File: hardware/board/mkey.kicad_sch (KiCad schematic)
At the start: 163 parts, among them J1 USB_C_REP_2.0, J2 24 pin LCD FPC connector, SW1 SW_Push, SW2 SW_Push, U1 ESP32-S3-WROOM-1, U5 SY8088

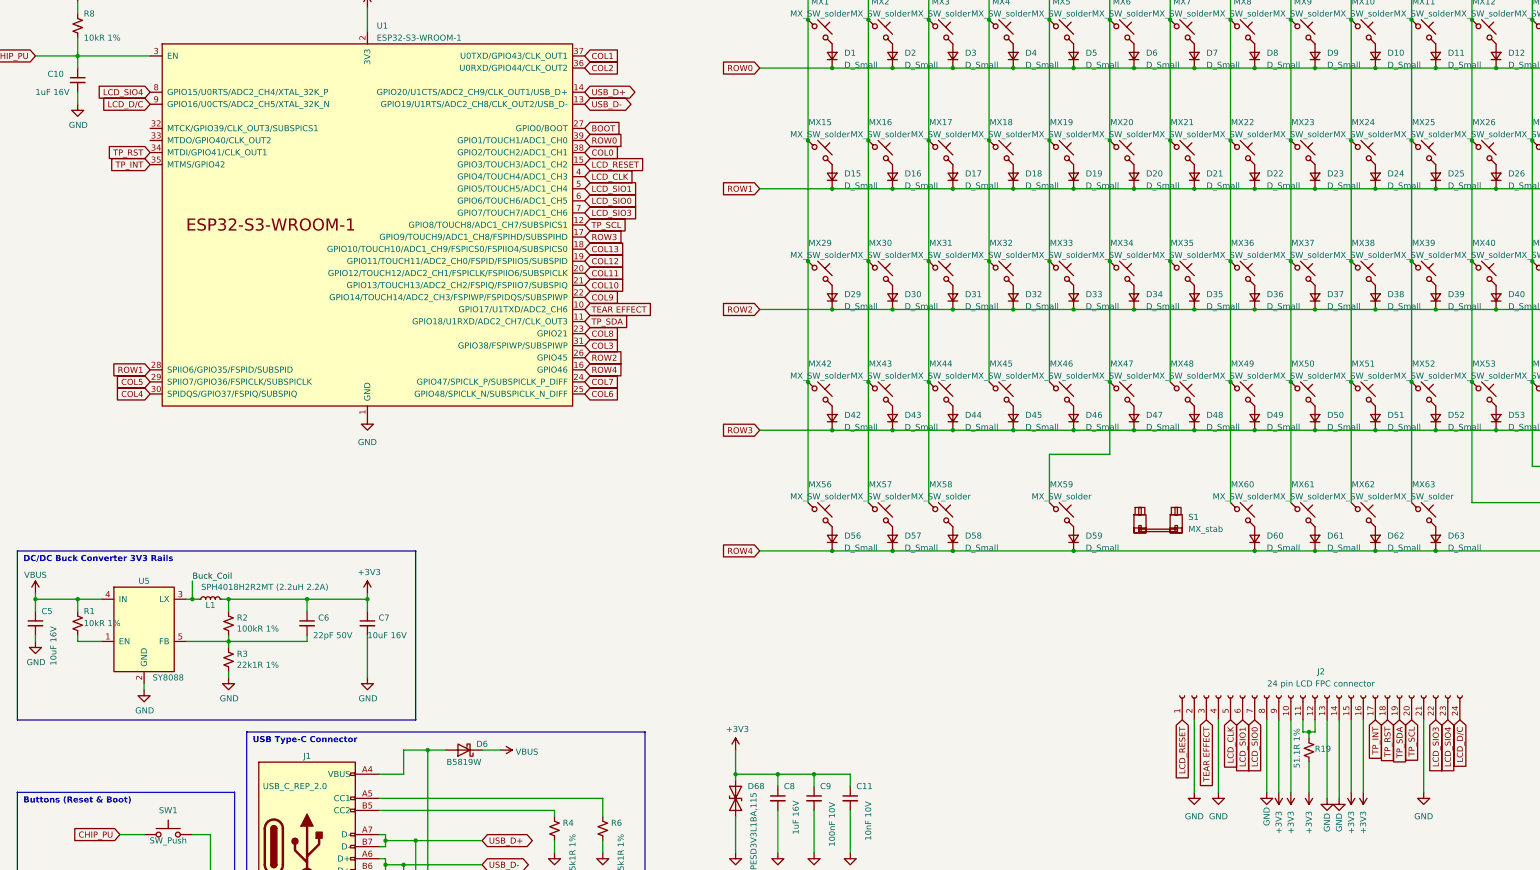
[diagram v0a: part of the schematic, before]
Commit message: hw: fix sio labels
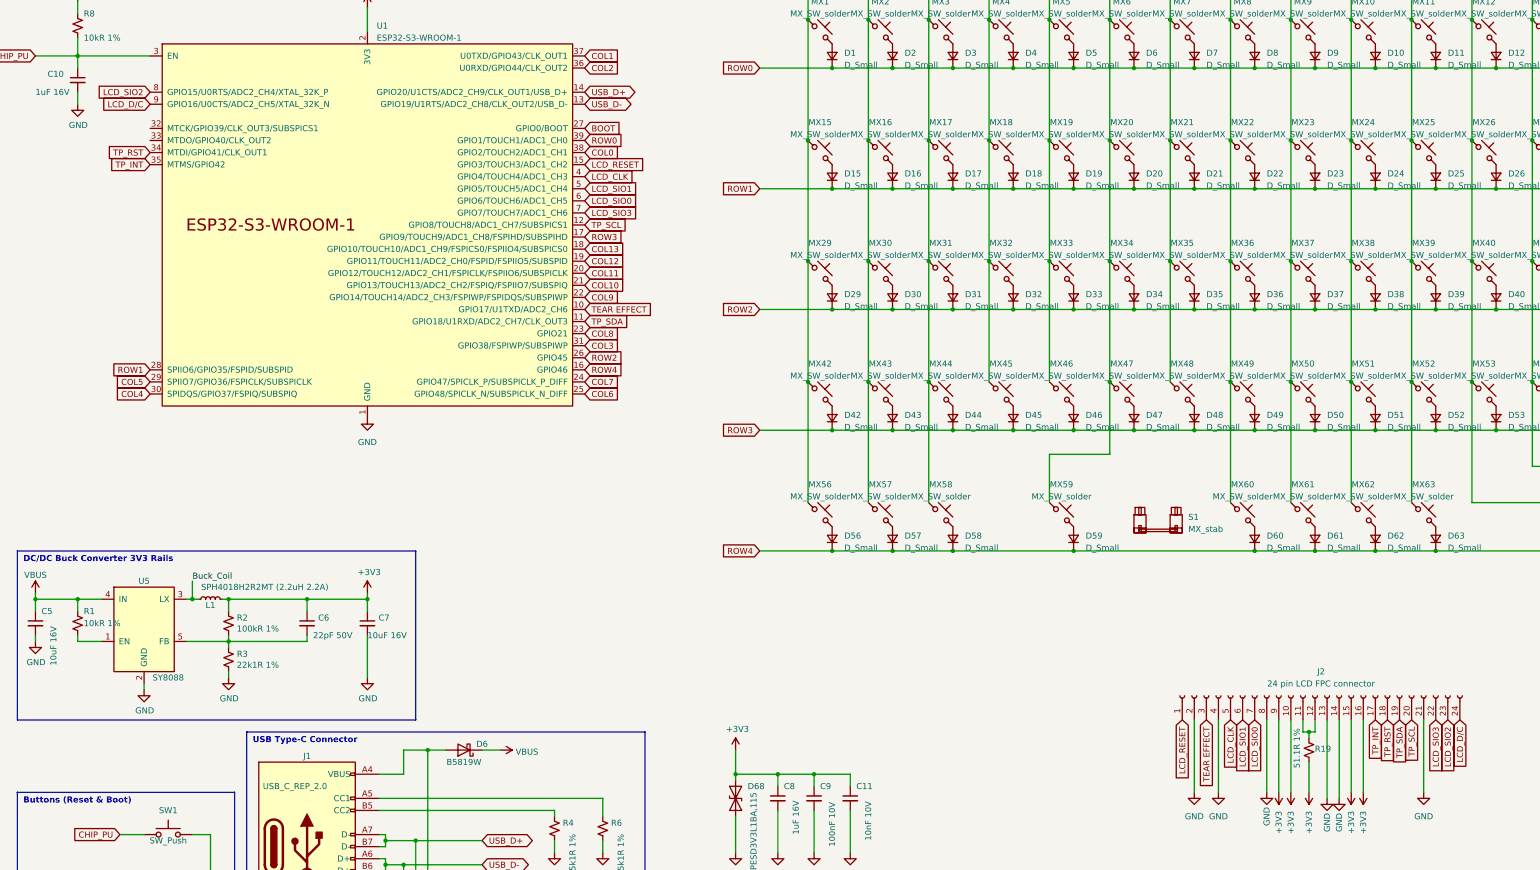
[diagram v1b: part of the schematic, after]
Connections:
- net LCD_SIO4 renamed LCD_SIO2
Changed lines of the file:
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@@
     )
   )
-  (global_label "LCD_SIO4" (shape input) (at 322.58 208.28 270) (fields_autoplaced)
+  (global_label "LCD_SIO2" (shape input) (at 322.58 208.28 270) (fields_autoplaced)
     (effects (font (size 1.27 1.27)) (justify right))
     (property "Intersheetrefs" "${INTERSHEET_REFS}" (at 322.58 220.1552 90)
@@
     )
   )
-  (global_label "LCD_SIO4" (shape input) (at 49.53 76.2 180) (fields_autoplaced)
+  (global_label "LCD_SIO2" (shape input) (at 49.53 76.2 180) (fields_autoplaced)
     (effects (font (size 1.27 1.27)) (justify right))
     (property "Intersheetrefs" "${INTERSHEET_REFS}" (at 37.6548 76.2 0)
